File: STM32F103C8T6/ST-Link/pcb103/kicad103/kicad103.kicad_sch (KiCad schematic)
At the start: 1 part, among them J1 USB_B_Micro

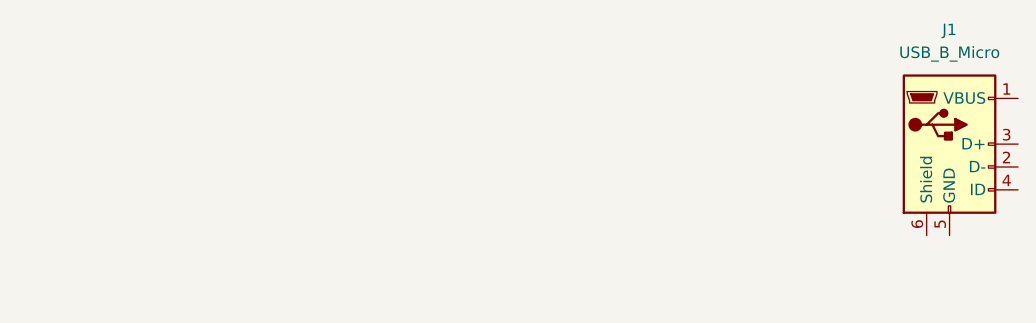
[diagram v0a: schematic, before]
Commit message: Add USB Type A
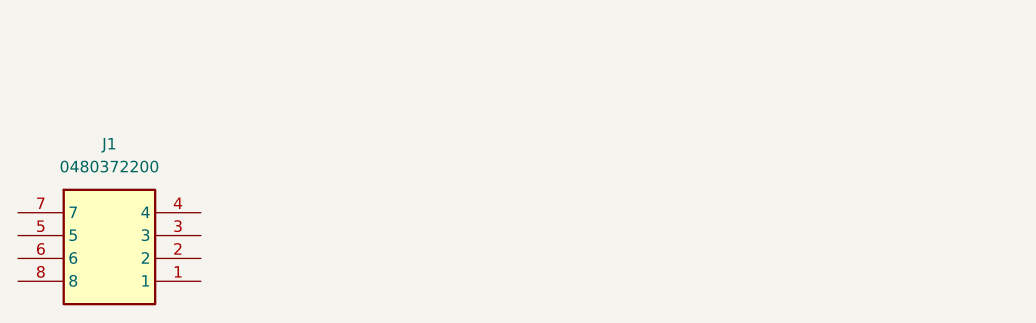
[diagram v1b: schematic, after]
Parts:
- removed J1: USB_B_Micro, Connector_USB:USB_Micro-B_Amphenol_10118193-0001LF_Horizontal, symbol Connector:USB_B_Micro
- added J1: 0480372200, Library:0480372200, symbol New_Library:0480372200
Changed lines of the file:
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@@
     (company "pvv")
   )
-  (symbol (lib_id "Connector:USB_B_Micro") (at 246.38 48.26 0) (unit 1)
+  (symbol (lib_id "New_Library:0480372200") (at 142.875 55.88 0) (unit 1)
     (in_bom yes) (on_board yes) (dnp no) (fields_autoplaced)
-    (property "Reference" "J1" (at 246.38 35.56 0)
+    (property "Reference" "J1" (at 153.035 48.26 0)
       (effects (font (size 1.27 1.27)))
     )
-    (property "Value" "USB_B_Micro" (at 246.38 38.1 0)
+    (property "Value" "0480372200" (at 153.035 50.8 0)
       (effects (font (size 1.27 1.27)))
     )
-    (property "Footprint" "Connector_USB:USB_Micro-B_Amphenol_10118193-0001LF_Horizontal" (at 250.19 49.53 0)
-      (effects (font (size 1.27 1.27)) hide)
+    (property "Footprint" "Library:0480372200" (at 159.385 150.8 0)
+      (effects (font (size 1.27 1.27)) (justify left top) hide)
     )
-    (property "Datasheet" "~" (at 250.19 49.53 0)
-      (effects (font (size 1.27 1.27)) hide)
+    (property "Datasheet" "https://www.molex.com/pdm_docs/sd/480372200_sd.pdf" (at 159.385 250.8 0)
+      (effects (font (size 1.27 1.27)) (justify left top) hide)
+    )
+    (property "Height" "4" (at 159.385 450.8 0)
+      (effects (font (size 1.27 1.27)) (justify left top) hide)
+    )
+    (property "Manufacturer_Name" "Molex" (at 159.385 550.8 0)
+      (effects (font (size 1.27 1.27)) (justify left top) hide)
+    )
+    (property "Manufacturer_Part_Number" "0480372200" (at 159.385 650.8 0)
+      (effects (font (size 1.27 1.27)) (justify left top) hide)
+    )
+    (property "Mouser Part Number" "N/A" (at 159.385 750.8 0)
+      (effects (font (size 1.27 1.27)) (justify left top) hide)
+    )
+    (property "Mouser Price/Stock" "https://www.mouser.co.uk/ProductDetail/Molex/0480372200?qs=PBcRNPEHKspH5weIJRN3iw%3D%3D" (at 159.385 850.8 0)
+      (effects (font (size 1.27 1.27)) (justify left top) hide)
+    )
+    (property "Arrow Part Number" "0480372200" (at 159.385 950.8 0)
+      (effects (font (size 1.27 1.27)) (justify left top) hide)
+    )
+    (property "Arrow Price/Stock" "https://www.arrow.com/en/products/0480372200/molex?region=nac" (at 159.385 1050.8 0)
+      (effects (font (size 1.27 1.27)) (justify left top) hide)
     )
     (pin "1")
@@
     (pin "5")
     (pin "6")
+    (pin "7")
+    (pin "8")
     (instances
       (project "kicad103"

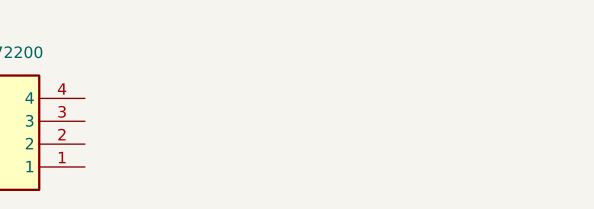
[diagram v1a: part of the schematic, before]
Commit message: Add 3.3V LDO
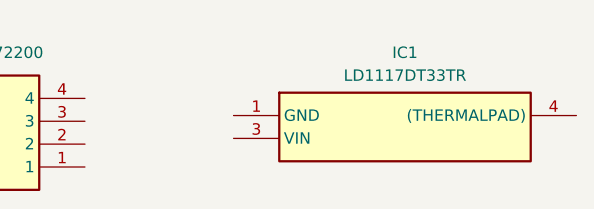
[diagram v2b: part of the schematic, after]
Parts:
- added IC1: LD1117DT33TR, Library:TO228P972X240-3N, symbol New_Library:LD1117DT33TR
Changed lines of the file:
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@@
     (company "pvv")
+  )
+  (symbol (lib_id "New_Library:LD1117DT33TR") (at 179.705 57.785 0) (unit 1)
+    (in_bom yes) (on_board yes) (dnp no) (fields_autoplaced)
+    (property "Reference" "IC1" (at 198.755 50.8 0)
+      (effects (font (size 1.27 1.27)))
+    )
+    (property "Value" "LD1117DT33TR" (at 198.755 53.34 0)
+      (effects (font (size 1.27 1.27)))
+    )
+    (property "Footprint" "Library:TO228P972X240-3N" (at 213.995 152.705 0)
+      (effects (font (size 1.27 1.27)) (justify left top) hide)
+    )
+    (property "Datasheet" "http://www.st.com/web/en/resource/technical/document/datasheet/CD00000544.pdf" (at 213.995 252.705 0)
+      (effects (font (size 1.27 1.27)) (justify left top) hide)
+    )
+    (property "Height" "2.4" (at 213.995 452.705 0)
+      (effects (font (size 1.27 1.27)) (justify left top) hide)
+    )
+    (property "Manufacturer_Name" "STMicroelectronics" (at 213.995 552.705 0)
+      (effects (font (size 1.27 1.27)) (justify left top) hide)
+    )
+    (property "Manufacturer_Part_Number" "LD1117DT33TR" (at 213.995 652.705 0)
+      (effects (font (size 1.27 1.27)) (justify left top) hide)
+    )
+    (property "Mouser Part Number" "511-LD1117DT33-TR" (at 213.995 752.705 0)
+      (effects (font (size 1.27 1.27)) (justify left top) hide)
+    )
+    (property "Mouser Price/Stock" "https://www.mouser.co.uk/ProductDetail/STMicroelectronics/LD1117DT33TR?qs=4JhUBQGAOSd4P5jVYGxp2g%3D%3D" (at 213.995 852.705 0)
+      (effects (font (size 1.27 1.27)) (justify left top) hide)
+    )
+    (property "Arrow Part Number" "LD1117DT33TR" (at 213.995 952.705 0)
+      (effects (font (size 1.27 1.27)) (justify left top) hide)
+    )
+    (property "Arrow Price/Stock" "https://www.arrow.com/en/products/ld1117dt33tr/stmicroelectronics?region=nac" (at 213.995 1052.705 0)
+      (effects (font (size 1.27 1.27)) (justify left top) hide)
+    )
+    (pin "1")
+    (pin "3")
+    (pin "4")
+    (instances
+      (project "kicad103"
+        (path "/185c057b-9149-49f2-8708-a9b3e40a18db"
+          (reference "IC1") (unit 1)
+        )
+      )
+    )
   )
   (symbol (lib_id "New_Library:0480372200") (at 142.875 55.88 0) (unit 1)

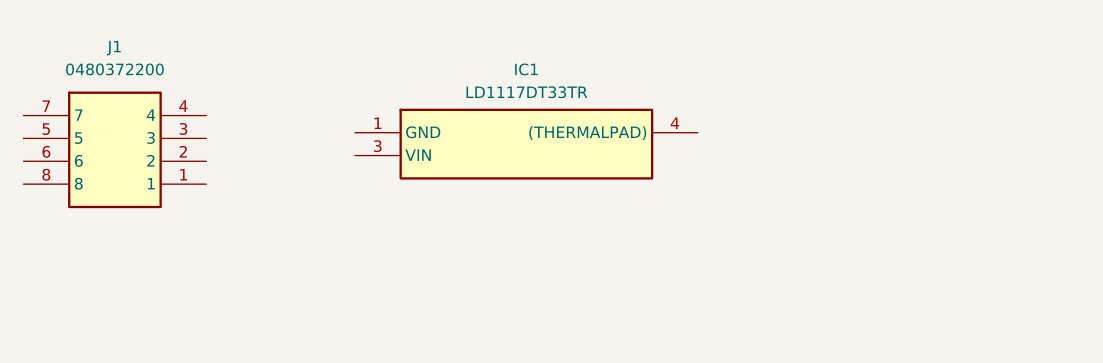
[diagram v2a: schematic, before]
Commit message: Add 3.3V power capacitors
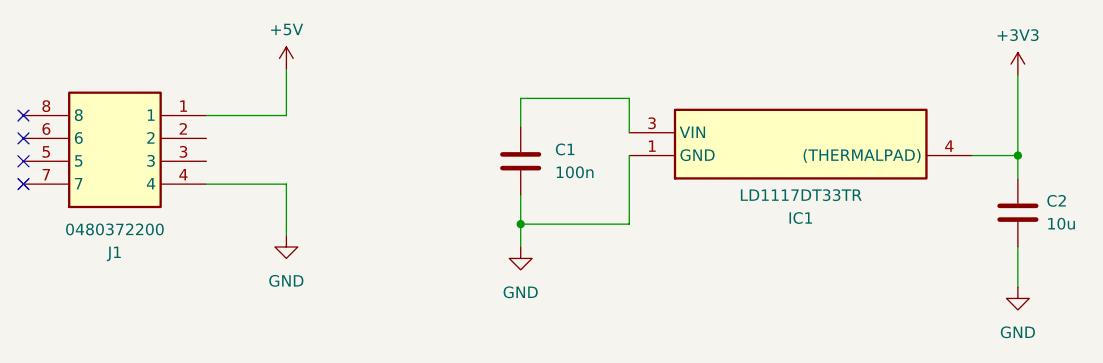
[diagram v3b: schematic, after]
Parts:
- added C1: 100n, Capacitor_SMD:C_1206_3216Metric, symbol Device:C
- added C2: 10u, Capacitor_SMD:C_0805_2012Metric, symbol Device:C
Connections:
- net GND: now reaches IC1.1 (GND)
- net GND: now also J1.4, C1.2, C2.2
- net at IC1.3 (VIN): now also C1.1
- net +3V3: now reaches IC1.4 ((THERMALPAD))
- net +3V3: now also C2.1
- net +5V: now reaches J1.1
- no-connect marks 0 -> 4
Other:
- moved on the sheet: IC1

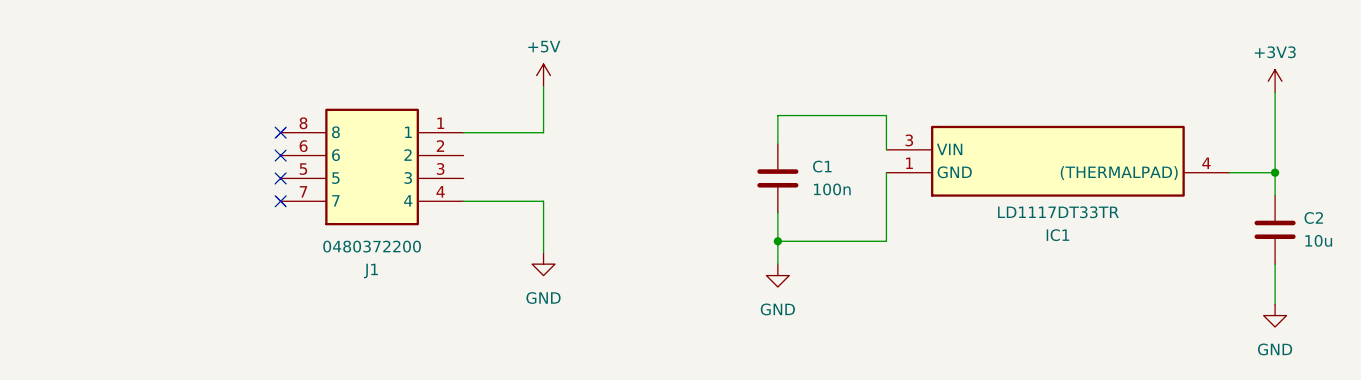
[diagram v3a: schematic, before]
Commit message: Add power header
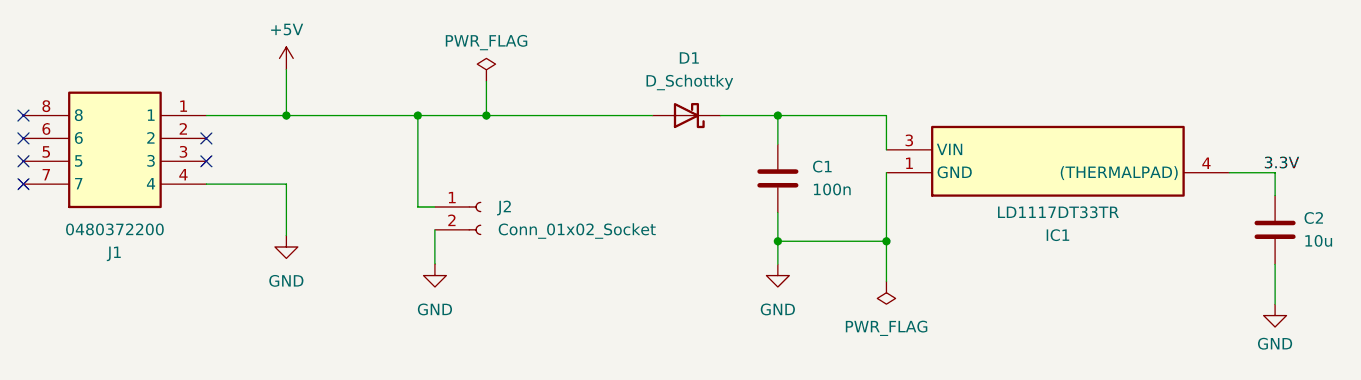
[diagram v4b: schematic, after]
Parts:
- added D1: D_Schottky, Diode_SMD:D_SOD-123, symbol Device:D_Schottky
- added J2: Conn_01x02_Socket, Connector_PinSocket_2.54mm:PinSocket_1x02_P2.54mm_Vertical, symbol Connector:Conn_01x02_Socket
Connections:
- net +5V: now also D1.2 (A), J2.1 (Pin_1)
- net GND: now also J2.2 (Pin_2)
- net at C1.1, IC1.3 (VIN): now also D1.1 (K)
- net +3V3 renamed 3.3V
- no-connect marks 4 -> 6
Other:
- moved on the sheet: J1

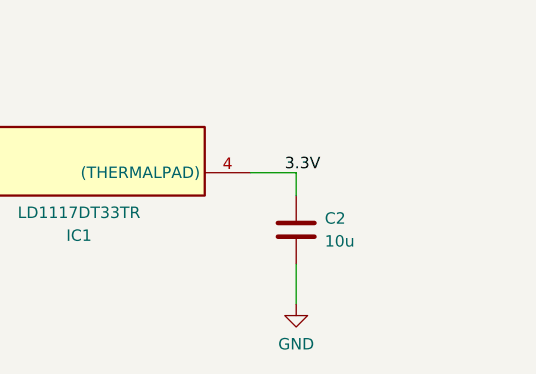
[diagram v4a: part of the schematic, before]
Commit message: Add power LED
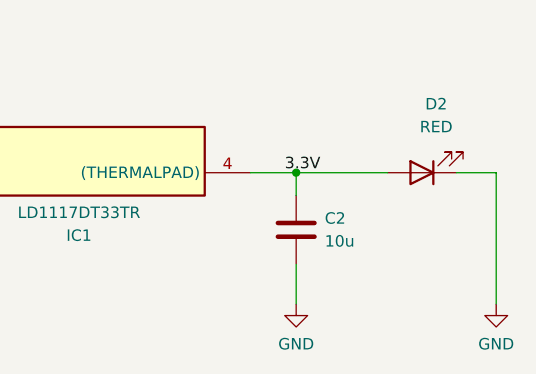
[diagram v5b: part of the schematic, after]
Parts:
- added D2: RED, LED_SMD:LED_0805_2012Metric, symbol Device:LED
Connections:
- net 3.3V: now also D2.2 (A)
- net GND: now also D2.1 (K)
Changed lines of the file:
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@@
   (junction (at 143.51 53.975) (diameter 0) (color 0 0 0 0)
+  )
+  (junction (at 253.365 60.325) (diameter 0) (color 0 0 0 0)
   )
   (junction (at 158.115 53.975) (diameter 0) (color 0 0 0 0)
@@
     (stroke (width 0) (type default))
   )
+  (wire (pts (xy 275.59 74.93) (xy 275.59 60.325))
+    (stroke (width 0) (type default))
+  )
   (wire (pts (xy 210.185 67.945) (xy 210.185 72.39))
     (stroke (width 0) (type default))
@@
   )
   (wire (pts (xy 134.62 53.975) (xy 143.51 53.975))
+    (stroke (width 0) (type default))
+  )
+  (wire (pts (xy 253.365 60.325) (xy 263.525 60.325))
+    (stroke (width 0) (type default))
+  )
+  (wire (pts (xy 275.59 60.325) (xy 271.145 60.325))
     (stroke (width 0) (type default))
   )
@@
         )
       )
+    )
+  )
+  (symbol (lib_id "power:GND") (at 275.59 74.93 0) (unit 1)
+    (in_bom yes) (on_board yes) (dnp no) (fields_autoplaced)
+    (property "Reference" "#PWR04" (at 275.59 81.28 0)
+      (effects (font (size 1.27 1.27)) hide)
+    )
+    (property "Value" "GND" (at 275.59 79.375 0)
+      (effects (font (size 1.27 1.27)))
+    )
+    (property "Footprint" "" (at 275.59 74.93 0)
+      (effects (font (size 1.27 1.27)) hide)
+    )
+    (property "Datasheet" "" (at 275.59 74.93 0)
+      (effects (font (size 1.27 1.27)) hide)
+    )
+    (pin "1")
+    (instances
+      (project "kicad103"
+        (path "/185c057b-9149-49f2-8708-a9b3e40a18db"
+          (reference "#PWR04") (unit 1)
+        )
+      )
+    )
+  )
+  (symbol (lib_id "Device:LED") (at 267.335 60.325 180) (unit 1)
+    (in_bom yes) (on_board yes) (dnp no) (fields_autoplaced)
+    (property "Reference" "D2" (at 268.9225 52.705 0)
+      (effects (font (size 1.27 1.27)))
+    )
+    (property "Value" "RED" (at 268.9225 55.245 0)
+      (effects (font (size 1.27 1.27)))
+    )
+    (property "Footprint" "LED_SMD:LED_0805_2012Metric" (at 267.335 60.325 0)
+      (effects (font (size 1.27 1.27)) hide)
+    )
+    (property "Datasheet" "~" (at 267.335 60.325 0)
+      (effects (font (size 1.27 1.27)) hide)
+    )
+    (pin "1")
+    (pin "2")
+    (instances
+      (project "kicad103"
+        (path "/185c057b-9149-49f2-8708-a9b3e40a18db"
+          (reference "D2") (unit 1)
+        )
+      )

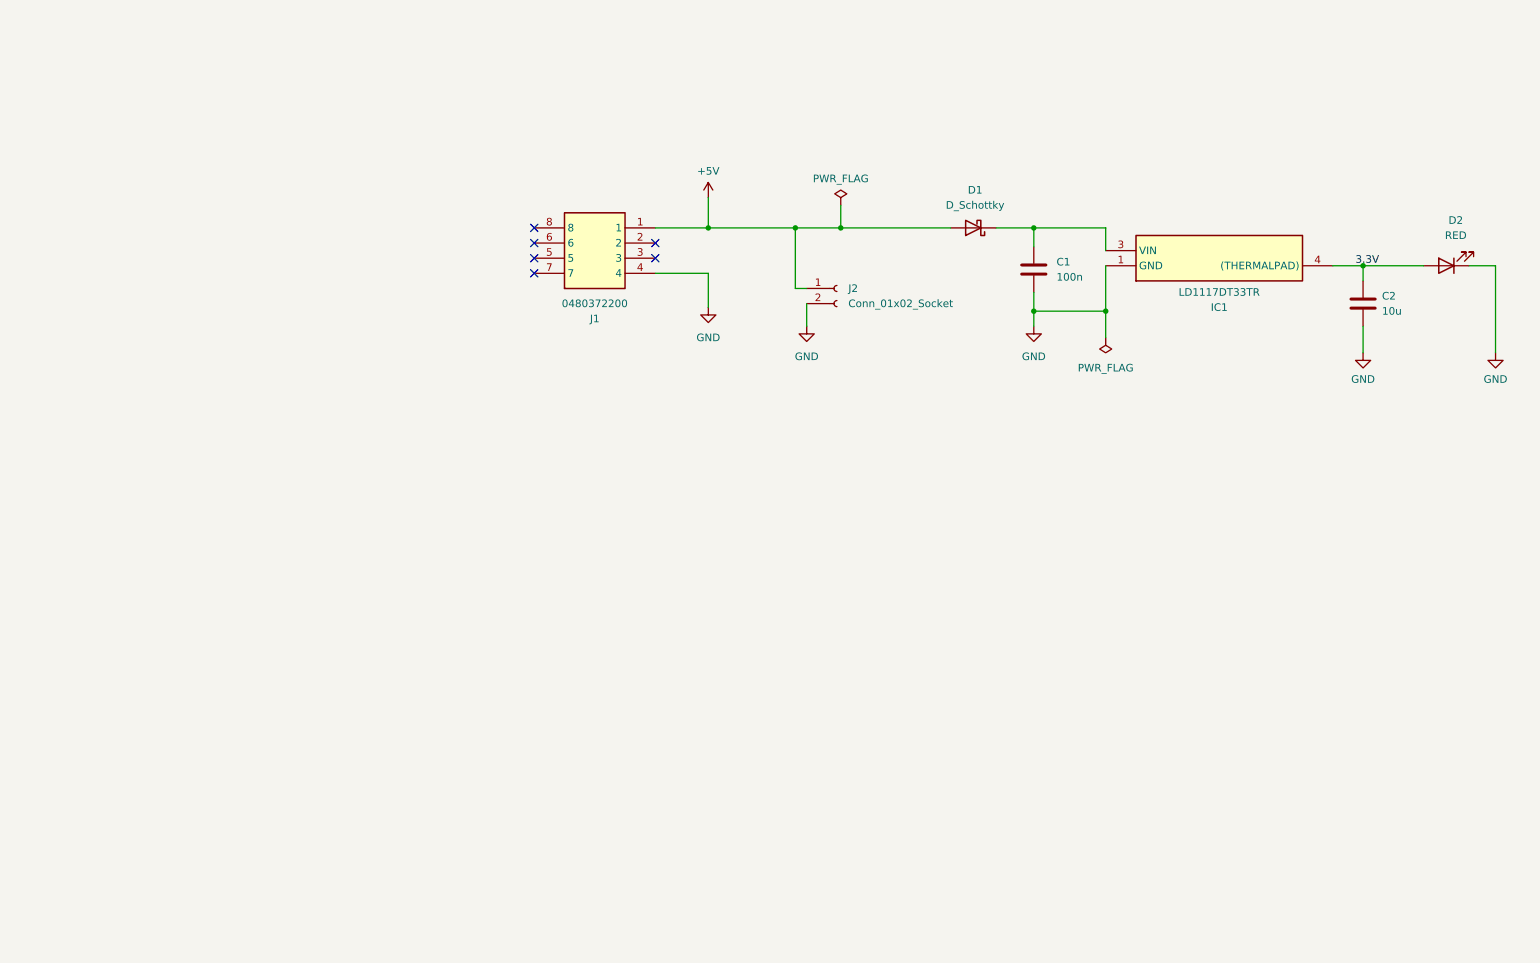
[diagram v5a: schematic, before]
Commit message: Add status LED
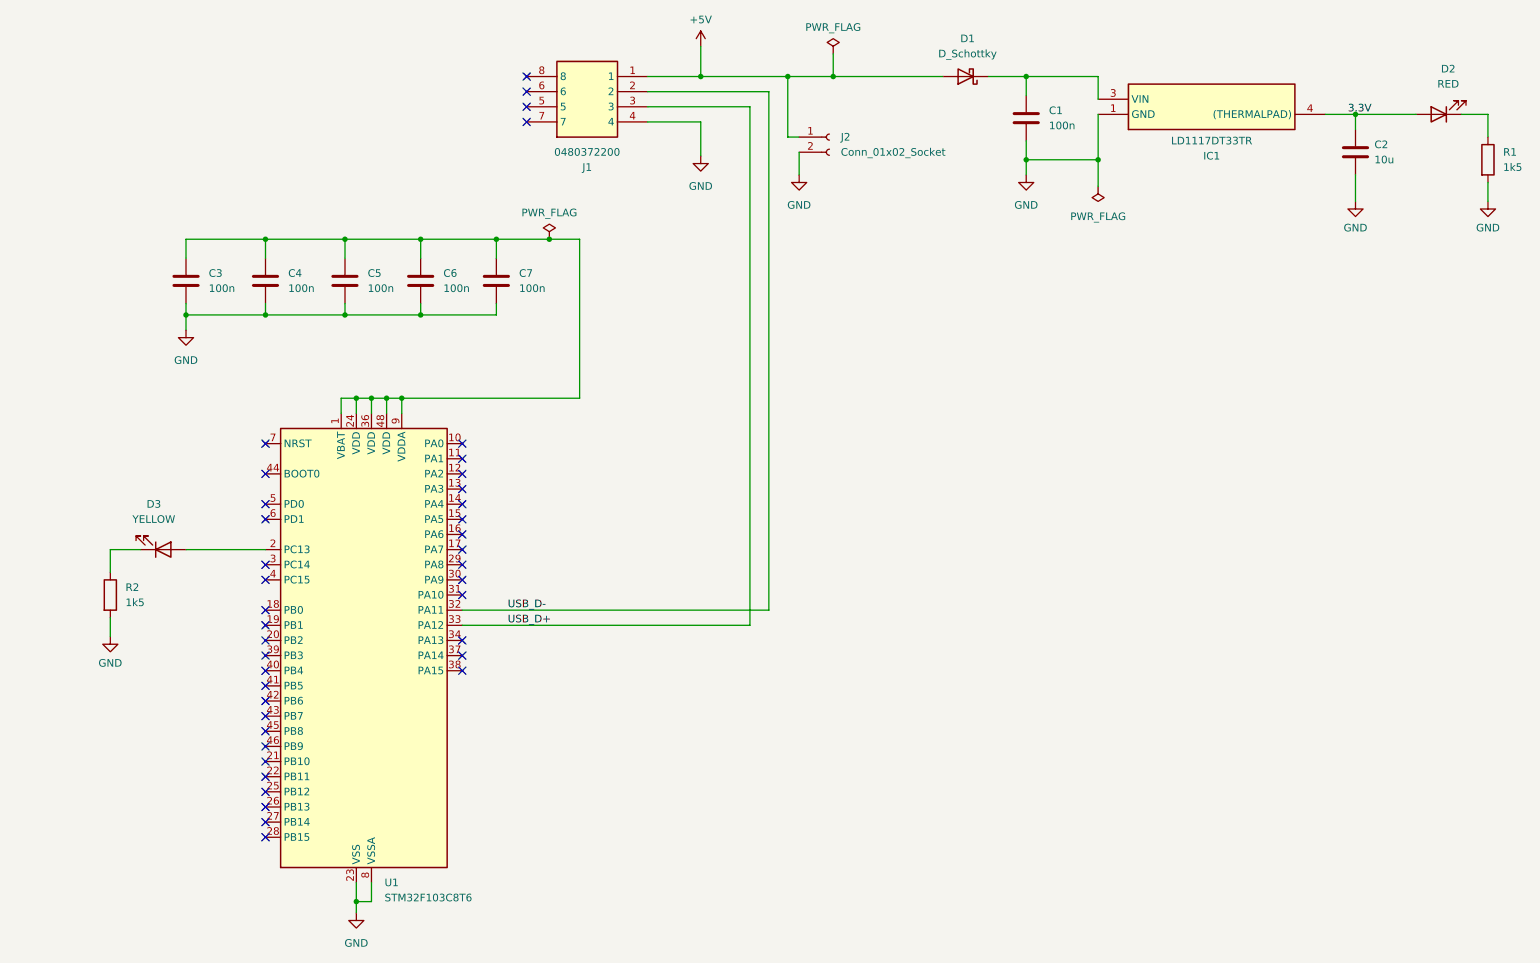
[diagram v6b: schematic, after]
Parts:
- added C3, C4, C5, C6, C7: 100n, Capacitor_SMD:C_0603_1608Metric, symbol Device:C
- added D3: YELLOW, LED_SMD:LED_0805_2012Metric, symbol Device:LED
- added R1, R2: 1k5, Resistor_SMD:R_0805_2012Metric, symbol Device:R
- added U1: STM32F103C8T6, Package_QFP:LQFP-48_7x7mm_P0.5mm, symbol MCU_ST_STM32F1:STM32F103C8Tx
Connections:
- net GND: now also C3.2, C4.2, C5.2, C6.2, C7.2, R1.2, R2.2, U1.23 (VSS), U1.35 (VSS), U1.47 (VSS), U1.8 (VSSA); no longer D2.1 (K)
- net USB_D-: now reaches J1.2
- net USB_D-: now also U1.32 (PA11)
- net USB_D+: now reaches J1.3
- net USB_D+: now also U1.33 (PA12)
- new net: C3.1, C4.1, C5.1, C6.1, C7.1, U1.1 (VBAT), U1.24 (VDD), U1.36 (VDD), U1.48 (VDD), U1.9 (VDDA)
- new net: D2.1 (K), R1.1
- new net: D3.1 (K), R2.1
- new net: D3.2 (A), U1.2 (PC13)
- no-connect marks 6 -> 40
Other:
- moved on the sheet: C1, C2, D1, D2, IC1, J1, J2
